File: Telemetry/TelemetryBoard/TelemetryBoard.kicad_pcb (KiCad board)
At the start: 2 copper layers, 44 parts, among them J1 Conn_01x07, J2 Conn_01x02, J3 Micro_SD_Card_Det, J4 Conn_01x04, J5 Conn_01x04, J6 Conn_02x08_Odd_Even, J7 Conn_02x15_Odd_Even, J8 Conn_02x10_Odd_Even, J9 Conn_02x17_Odd_Even, U2 ADM3055E, U3 PQMC3-Dx-Sx-S, U4 CDSOT23-T24CAN

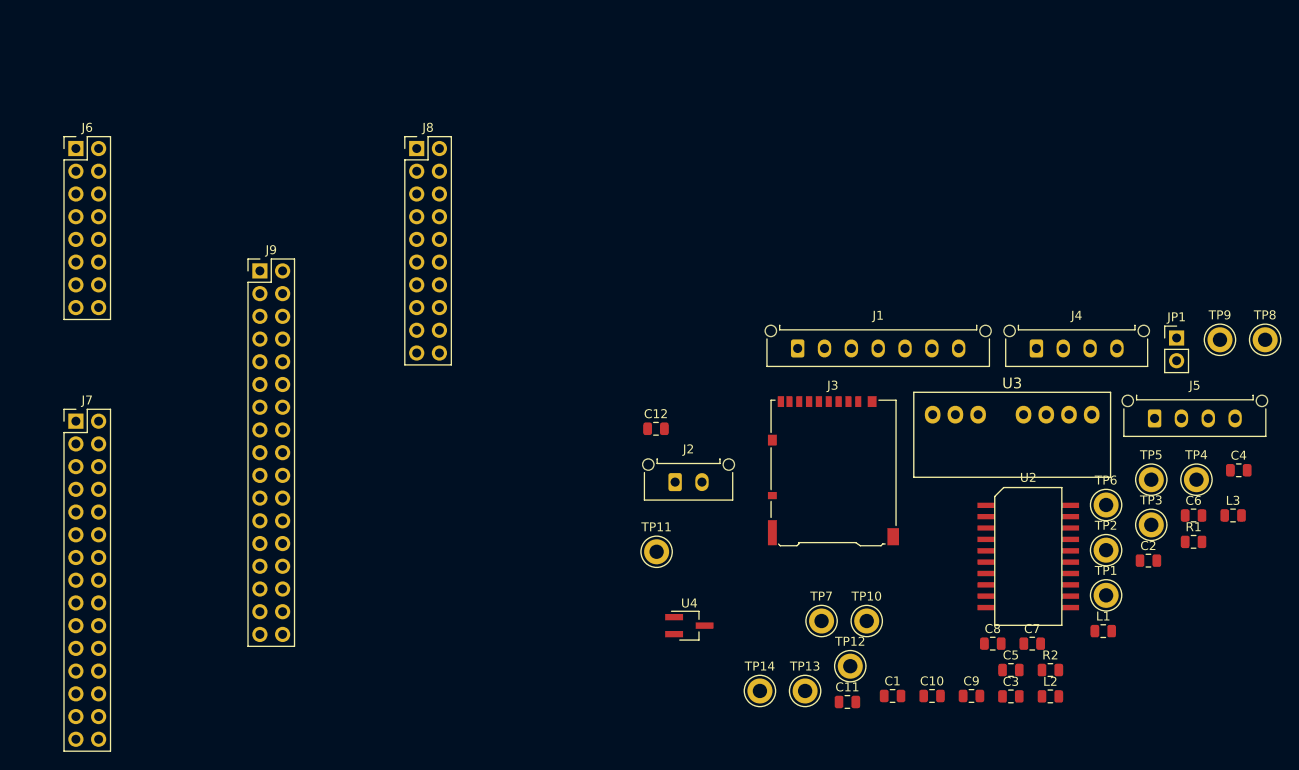
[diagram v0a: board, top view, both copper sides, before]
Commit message: Editing Array Board and telemetry board
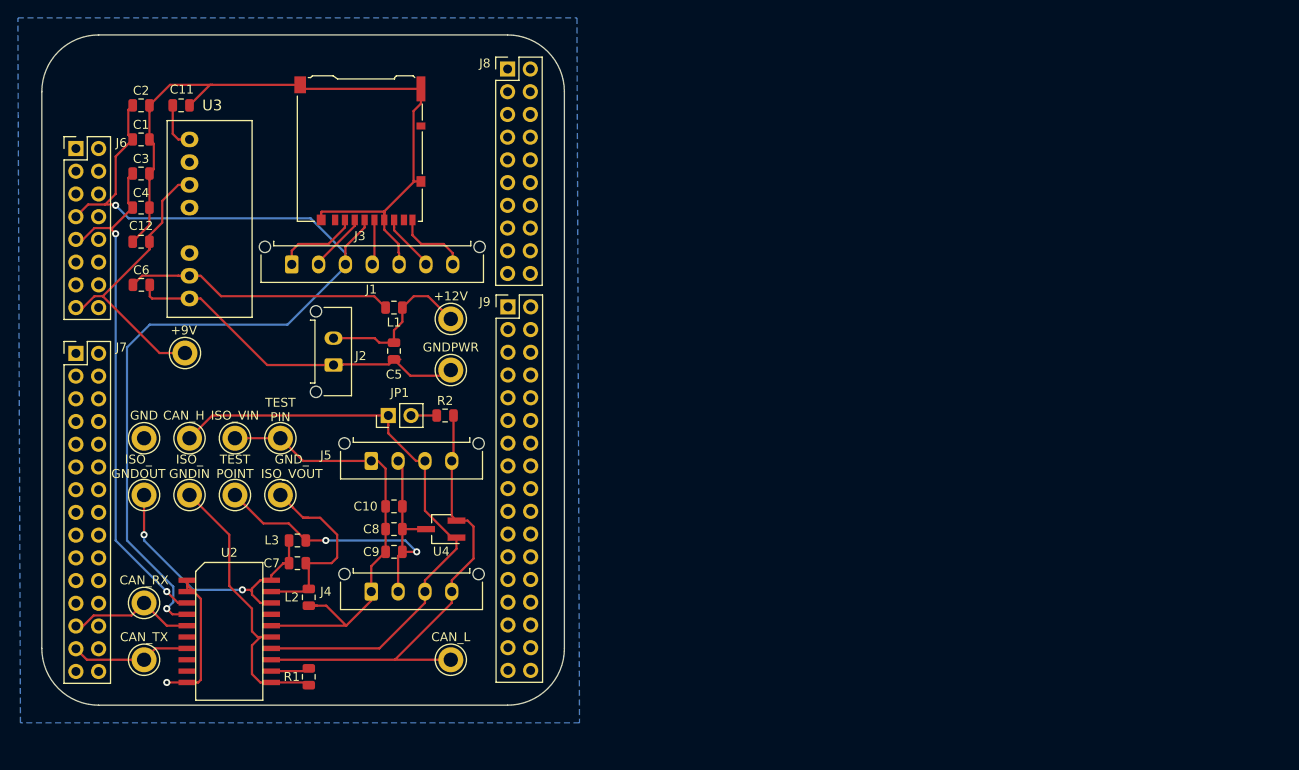
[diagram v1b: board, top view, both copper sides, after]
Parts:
- moved TP8 126.5 mm to (83.8, 89.5)
- moved C4 126.2 mm to (83.5, 57.4)
- moved C2 123.6 mm to (83.5, 46.0)
- moved C6 120.4 mm to (83.5, 66.0)
- moved TP9 115.7 mm to (88.9, 83.2)
- moved C3 113.5 mm to (83.5, 53.6)
- moved TP1 107.8 mm to (83.8, 108.0)
- moved TP2 107.7 mm to (83.8, 101.6)
- moved L3 104.6 mm to (101.0, 94.6), turned to 180 degrees
- moved C1 104.5 mm to (83.5, 49.8)
- moved TP5 102.5 mm to (94.0, 83.2)
- moved R1 100.1 mm to (102.2, 109.9), turned to 90 degrees
- moved C11 100.0 mm to (88.0, 46.0)
- moved U3 94.5 mm to (88.9, 58.7), turned to 90 degrees
- moved TP6 92.3 mm to (99.1, 89.5)
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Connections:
- R1 pad 1: Net-(C7-Pad2) -> Net-(R1-Pad1)
- TP7 pad 1: Net-(C7-Pad2) -> Net-(R1-Pad1)
- U2 pad 11: Net-(C7-Pad2) -> Net-(R1-Pad1)
- U2 pad 15: Net-(C7-Pad2) -> Net-(R1-Pad1)
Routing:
- net +3V3: track 0.00 -> 115.4 mm, vias 0 -> 2
- net GND: track 0.00 -> 100.0 mm, vias 0 -> 1
- net Net-(J4-Pad3): track 0.00 -> 69.6 mm
- net +5V: track 0.00 -> 58.1 mm, vias 0 -> 2
- net Net-(J4-Pad4): track 0.00 -> 52.7 mm
- net Net-(C10-Pad1): track 0.00 -> 52.1 mm
- net Net-(C10-Pad2): track 0.00 -> 42.2 mm, vias 0 -> 2
- net GNDPWR: track 0.00 -> 40.1 mm
- net Net-(R1-Pad1): track 0.00 -> 33.2 mm
- net +9V: track 0.00 -> 32.5 mm
- net Net-(C7-Pad2): track 0.00 -> 31.2 mm, vias 0 -> 2
- net Net-(C6-Pad1): track 0.00 -> 30.1 mm
- net Net-(C7-Pad1): track 0.00 -> 22.3 mm
- net +12V: track 0.00 -> 18.3 mm
- net /CAN_RD: track 0.00 -> 14.6 mm
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- added copper zone on B.Cu, net GND
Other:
- board outline added: 58.4 x 74.9 mm
- board text added: "+12V"
- board text added: "+9V"
- board text added: "CAN_H"
- board text added: "CAN_L"
- board text added: "CAN_RX"
- board text added: "CAN_TX"
- board text added: "GND"
- board text added: "GNDPWR"
- board text added: "GND_ ISO_VOUT"
- board text added: "ISO_ GNDIN"
- board text added: "ISO_ GNDOUT"
- board text added: "ISO_VIN"
- board text added: "TEST PIN"
- board text added: "TEST POINT"

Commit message: Finished Telemetry Board
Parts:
- removed J1: Conn_01x07, Connector_Molex:Molex_Micro-Fit_3.0_43650-0715_1x07_P3.00mm_Vertical
- removed TP11, TP12: TestPoint, TestPoint:TestPoint_Keystone_5005-5009_Compact
- added D1: LED, LED_SMD:LED_0805_2012Metric, F.Cu at (100.6, 61.2)
- added G***: LOGO, UTSVT_Special:Hallock_Image_Small, B.Cu at (101.0, 52.5)
- added G***: LOGO, UTSVT_Special:UTSVT_Logo_Symbol, F.Cu at (82.4, 42.3)
- added R3: 3k, Resistor_SMD:R_0805_2012Metric, F.Cu at (100.6, 57.6)
- L1: footprint Inductor_SMD:L_0805_2012Metric -> Inductor_SMD:L_TDK_NLV32_3.2x2.5mm
- moved TP14 13.5 mm to (97.2, 81.3)
- moved TP9 9.25 mm to (91.4, 74.3)
- moved TP8 8.47 mm to (85.7, 81.3)
- moved TP6 7.72 mm to (91.5, 88.3)
- moved C10 6.53 mm to (105.2, 90.9), turned to 180 degrees
- moved J3 5.36 mm to (110.7, 46.5)
- moved J4 3.75 mm to (105.9, 102.1)
- moved J5 3.46 mm to (105.8, 85.9)
- moved TP7 3.42 mm to (85.7, 88.3)
- moved TP5 3.17 mm to (91.4, 81.3)
- moved TP13 2.74 mm to (85.7, 74.3)
- moved L2 2.71 mm to (100.7, 103.2)
- moved J9 2.58 mm to (121.9, 68.6)
- moved J8 2.54 mm to (121.9, 41.9)
- moved U3 1.91 mm to (90.8, 58.7)
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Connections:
- J3 pad 2: Net-(J1-Pad1) -> /CS
- J3 pad 3: Net-(J1-Pad2) -> /MOSI
- J3 pad 5: Net-(J1-Pad4) -> /CLOCK
- J3 pad 7: Net-(J1-Pad6) -> /MISO
- J3 pad 9: Net-(J1-Pad7) -> /DET
- J8 pad 10: Net-(J8-Pad10) -> /CLOCK
- J8 pad 12: Net-(J8-Pad12) -> /MISO
- J8 pad 14: Net-(J8-Pad14) -> /MOSI
- J8 pad 16: Net-(J8-Pad16) -> /CS
- J8 pad 20: Net-(J8-Pad20) -> /DET
- J8 pad 8: Net-(J8-Pad8) -> GND
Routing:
- net GND: track 100.0 -> 29.8 mm, vias 1 -> 0
- net /DET: track 0.00 -> 20.1 mm, vias 0 -> 2
- net /CS: track 0.00 -> 19.3 mm
- net /CLOCK: track 0.00 -> 18.1 mm, vias 0 -> 2
- net /MOSI: track 0.00 -> 17.1 mm
- net +9V: track 32.5 -> 48.6 mm
- net Net-(C7-Pad2): track 31.2 -> 44.2 mm
- net /MISO: track 0.00 -> 12.2 mm
- net Net-(J1-Pad1): track 9.40 -> 0.00 mm
- net Net-(J1-Pad7): track 8.30 -> 0.00 mm
- net Net-(C10-Pad1): track 52.1 -> 45.1 mm
- net Net-(J1-Pad2): track 6.65 -> 0.00 mm
- net +3V3: track 115.4 -> 108.9 mm, vias 2 -> 3
- net Net-(J1-Pad6): track 6.45 -> 0.00 mm
- net Net-(J1-Pad4): track 5.08 -> 0.00 mm
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- added copper zone on F.Cu, net GND
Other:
- board size 58.4 x 74.9 mm -> 55.9 x 74.9 mm
- board text added: "Hannah Was Here"
- board text added: "Termination Resistors"
- board text added: "UTSVT Telemetry v1.0 Spring 2020"
- board text removed: "TEST PIN"
- board text removed: "TEST POINT"
